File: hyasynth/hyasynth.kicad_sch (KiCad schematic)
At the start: 38 parts, among them J1 Conn_01x04_Male, J2 Conn_01x02_Male, J3 Conn_01x07_Male, J4 Conn_01x02_Male, J5 Conn_01x02_Male, J6 AudioJack3_SwitchTR, SW1 Power Switch, SW10 G# Ab, SW11 A, SW12 A# Bb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

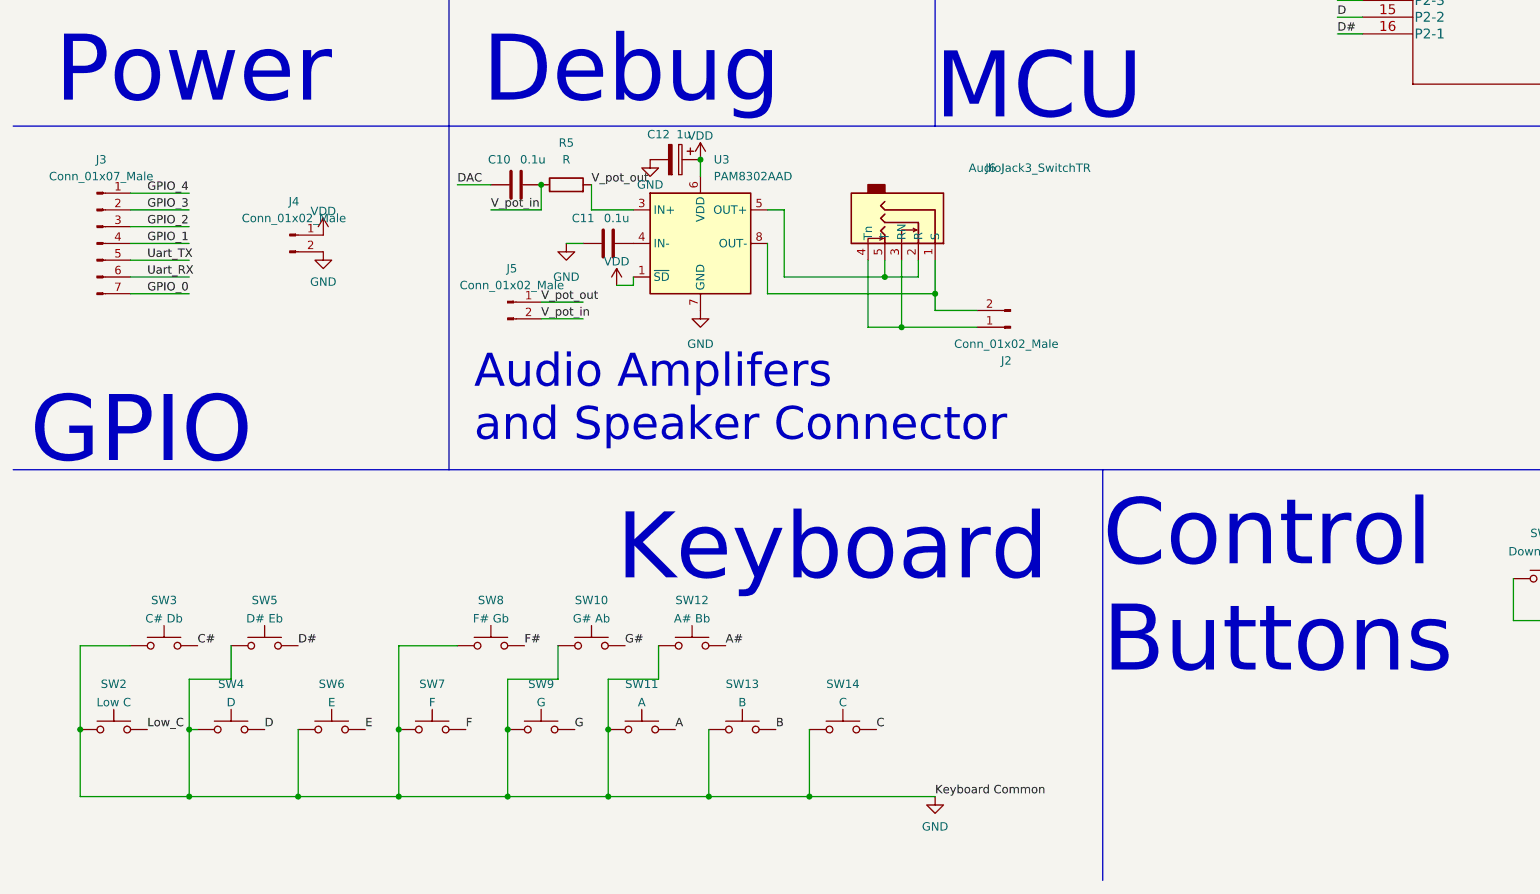
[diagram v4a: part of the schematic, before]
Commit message: Finished Basic Revision of PCB
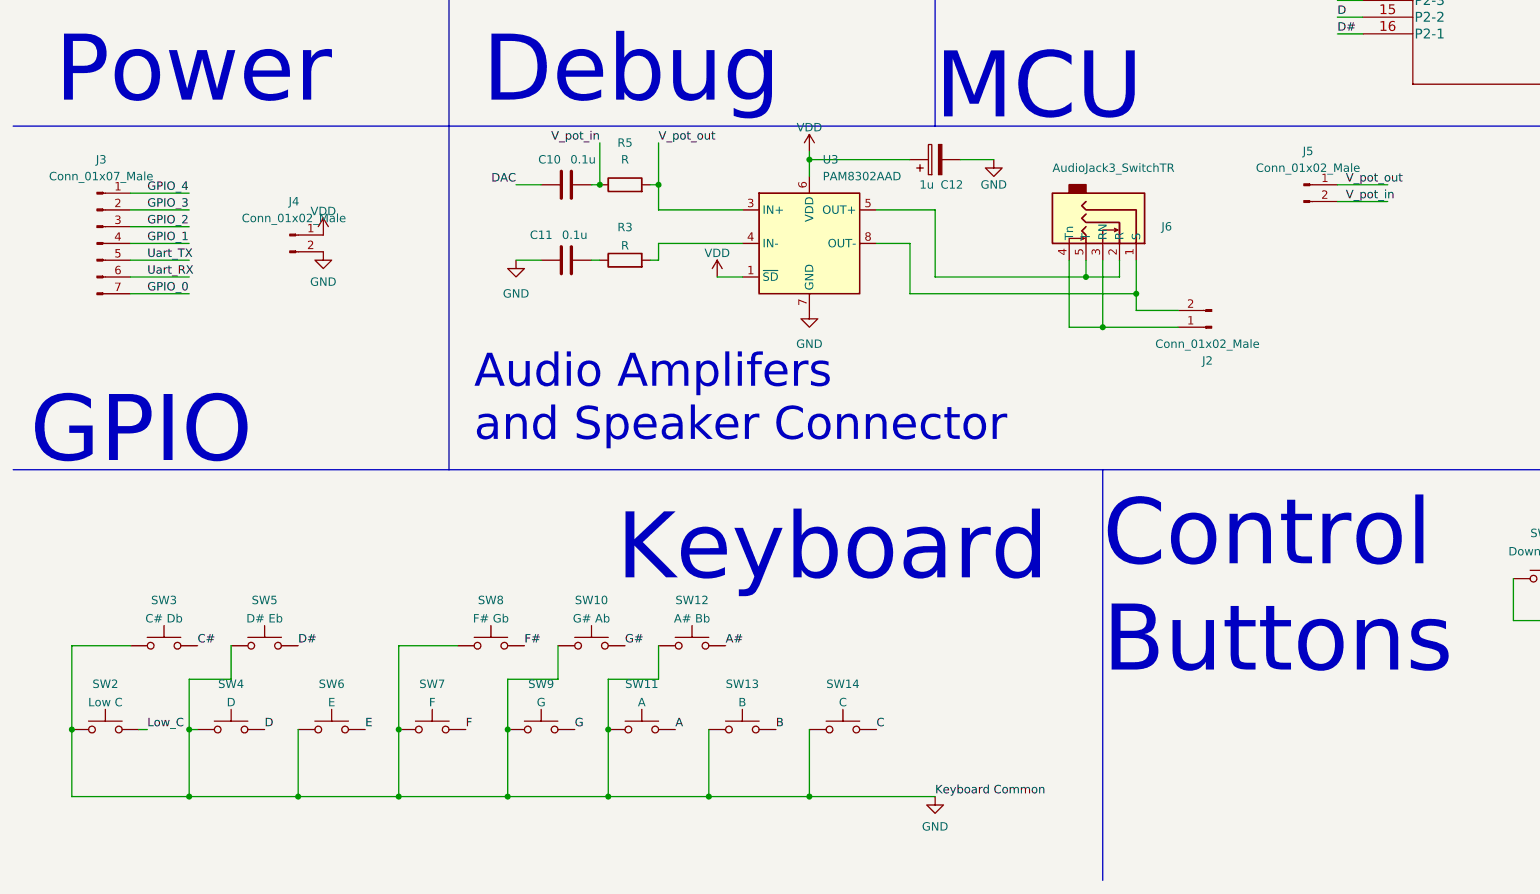
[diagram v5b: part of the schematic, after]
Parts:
- added R3: R, Resistor_SMD:R_0805_2012Metric_Pad1.20x1.40mm_HandSolder, symbol Device:R
- SW10, SW11, SW12, SW13, SW14, SW15, SW16, SW17, SW18, SW2, SW3, SW4, SW5, SW6, SW7, SW8, SW9: footprint Button_Switch_SMD:SW_Push_1P1T_NO_CK_KSC7xxJ -> Button:SW_Push_hand_solder
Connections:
- net at C11.2: now also R3.1; no longer U3.4 (IN-)
- new net: R3.2, U3.4 (IN-)
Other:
- moved on the sheet: C10, C11, C12, J2, J5, J6, R5, SW2, U3

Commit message: Schematic Changes
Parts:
- removed R1: 10K, Resistor_SMD:R_0805_2012Metric_Pad1.20x1.40mm_HandSolder, symbol Device:R
- removed R2: 1K, Resistor_SMD:R_0805_2012Metric_Pad1.20x1.40mm_HandSolder, symbol Device:R
- removed SW18: Reset, Button:SW_Push_hand_solder, symbol Switch:SW_Push
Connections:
- net GND: no longer U1.9 (P3-1)
- net VDD: no longer U3.1 (~{SD})
- net AMP_OUT-: now reaches J2.2 (Pin_2), J6.1 (S), U3.8 (OUT-)
- net AMP_OUT+: now reaches J6.2 (R), J6.5 (T), U3.5 (OUT+)
- net SPK_OUT-: now reaches J2.1 (Pin_1), J6.3 (RN), J6.4 (Tn)
- new net AMP_SD: U1.9 (P3-1), U3.1 (~{SD})

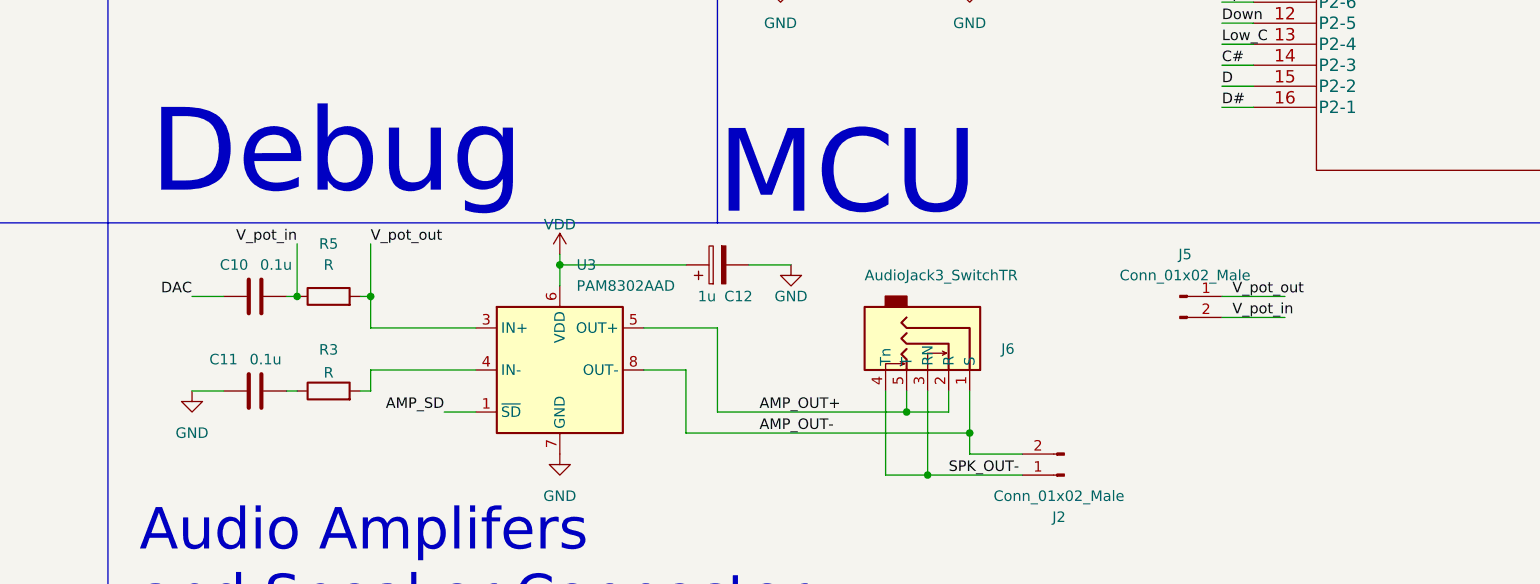
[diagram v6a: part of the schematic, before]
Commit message: tweaks for printing
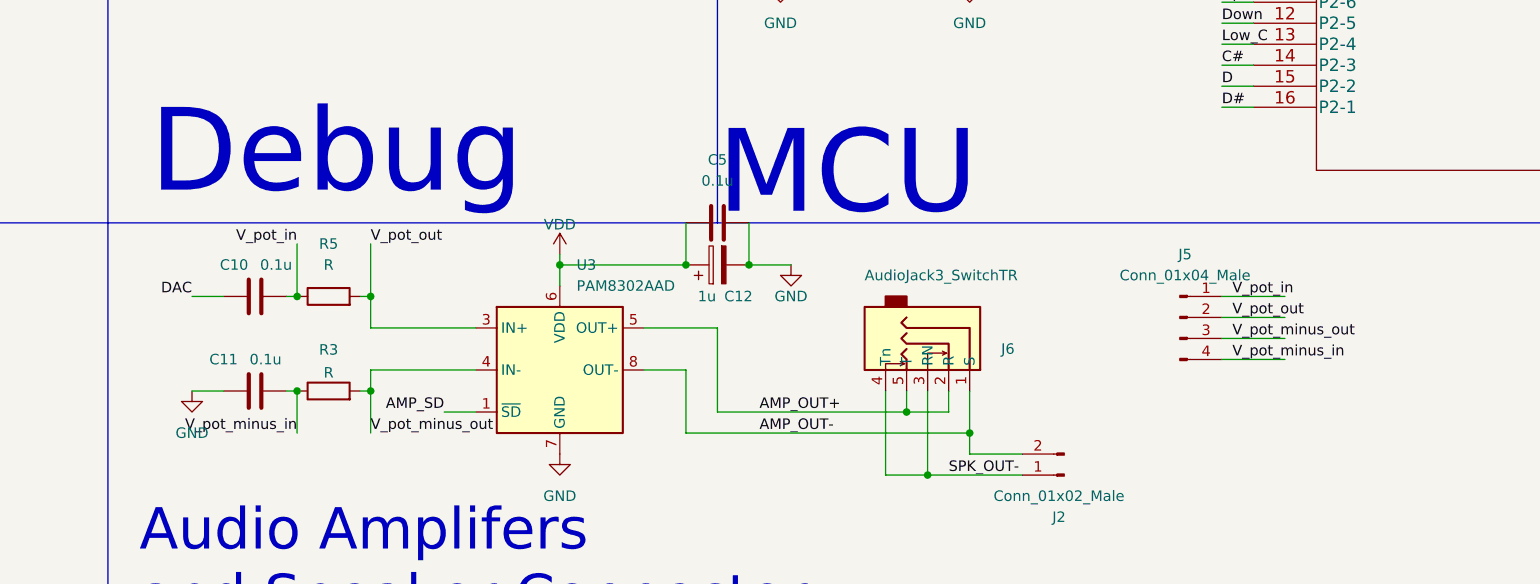
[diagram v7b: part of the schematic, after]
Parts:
- removed J5: Conn_01x02_Male, Connector_PinHeader_2.54mm:PinHeader_1x02_P2.54mm_Vertical, symbol Connector:Conn_01x02_Male
- added C5: 0.1u, Capacitor_SMD:C_0805_2012Metric_Pad1.18x1.45mm_HandSolder, symbol Device:C
- added J5: Conn_01x04_Male, Connector_PinHeader_2.54mm:PinHeader_1x04_P2.54mm_Vertical, symbol Connector:Conn_01x04_Male
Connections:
- net GND: now also C5.2
- net VDD: now also C5.1
- net V_pot_in: now also J5.1 (Pin_1)
- net V_pot_out: now also J5.2 (Pin_2)
- net V_pot_minus_in: now reaches C11.2, R3.1
- net V_pot_minus_in: now also J5.4 (Pin_4)
- net V_pot_minus_out: now reaches R3.2, U3.4 (IN-)
- net V_pot_minus_out: now also J5.3 (Pin_3)
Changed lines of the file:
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@@
   (junction (at 132.08 185.42) (diameter 0) (color 0 0 0 0)
   )
+  (junction (at 154.94 88.9) (diameter 0) (color 0 0 0 0)
+  )
   (junction (at 176.53 114.3) (diameter 0) (color 0 0 0 0)
   )
@@
   (junction (at 20.32 175.26) (diameter 0) (color 0 0 0 0)
   )
+  (junction (at 100.33 104.14) (diameter 0) (color 0 0 0 0)
+  )
   (junction (at 69.85 175.26) (diameter 0) (color 0 0 0 0)
   )
@@
   (junction (at 181.61 48.26) (diameter 0) (color 0 0 0 0)
   )
+  (junction (at 147.32 88.9) (diameter 0) (color 0 0 0 0)
+  )
   (junction (at 101.6 185.42) (diameter 0) (color 0 0 0 0)
   )
@@
   (junction (at 86.36 175.26) (diameter 0) (color 0 0 0 0)
   )
+  (junction (at 109.22 104.14) (diameter 0) (color 0 0 0 0)
+  )
   (junction (at 100.33 92.71) (diameter 0) (color 0 0 0 0)
   )
@@
     (stroke (width 0) (type default) (color 0 0 0 0))
   )
+  (wire (pts (xy 109.22 104.14) (xy 109.22 109.22))
+    (stroke (width 0) (type default) (color 0 0 0 0))
+  )
   (wire (pts (xy 173.99 106.68) (xy 179.07 106.68))
     (stroke (width 0) (type default) (color 0 0 0 0))
@@
     (stroke (width 0) (type default) (color 0 0 0 0))
   )
+  (wire (pts (xy 147.32 83.82) (xy 147.32 88.9))
+    (stroke (width 0) (type default) (color 0 0 0 0))
+  )
   (wire (pts (xy 181.61 40.64) (xy 193.04 40.64))
     (stroke (width 0) (type default) (color 0 0 0 0))
@@
     (stroke (width 0) (type default) (color 0 0 0 0))
   )
+  (wire (pts (xy 100.33 104.14) (xy 100.33 109.22))
+    (stroke (width 0) (type default) (color 0 0 0 0))
+  )
   (wire (pts (xy 158.75 40.64) (xy 170.18 40.64))
     (stroke (width 0) (type default) (color 0 0 0 0))
@@
     (stroke (width 0) (type default) (color 0 0 0 0))
   )
+  (wire (pts (xy 154.94 83.82) (xy 154.94 88.9))
+    (stroke (width 0) (type default) (color 0 0 0 0))
+  )
   (wire (pts (xy 212.09 44.45) (xy 215.9 44.45))
     (stroke (width 0) (type default) (color 0 0 0 0))
@@
     (stroke (width 0) (type default) (color 0 0 0 0))
   )
+  (wire (pts (xy 212.09 97.79) (xy 219.71 97.79))
+    (stroke (width 0) (type default) (color 0 0 0 0))
+  )
   (wire (pts (xy 187.96 111.76) (xy 181.61 111.76))
     (stroke (width 0) (type default) (color 0 0 0 0))
@@
   )
   (wire (pts (xy 99.06 92.71) (xy 100.33 92.71))
+    (stroke (width 0) (type default) (color 0 0 0 0))
+  )
+  (wire (pts (xy 212.09 100.33) (xy 219.71 100.33))
     (stroke (width 0) (type default) (color 0 0 0 0))
   )
@@
     (effects (font (size 1.27 1.27)) (justify right bottom))
   )
+  (label "V_pot_minus_in" (at 100.33 109.22 180)
+    (effects (font (size 1.27 1.27)) (justify right bottom))
+  )
   (label "A#" (at 266.7 57.15 0)
     (effects (font (size 1.27 1.27)) (justify left bottom))
@@
     (effects (font (size 1.27 1.27)) (justify left bottom))
   )
+  (label "V_pot_minus_in" (at 213.36 100.33 0)
+    (effects (font (size 1.27 1.27)) (justify left bottom))
+  )
   (label "AMP_OUT-" (at 156.21 109.22 0)
     (effects (font (size 1.27 1.27)) (justify left bottom))
@@
     (effects (font (size 1.27 1.27)) (justify left bottom))
   )
+  (label "V_pot_minus_out" (at 109.22 109.22 0)
+    (effects (font (size 1.27 1.27)) (justify left bottom))
+  )
   (label "D#" (at 212.09 69.85 0)
     (effects (font (size 1.27 1.27)) (justify left bottom))
@@
   )
   (label "A" (at 111.76 175.26 0)
+    (effects (font (size 1.27 1.27)) (justify left bottom))
+  )
+  (label "V_pot_minus_out" (at 213.36 97.79 0)
     (effects (font (size 1.27 1.27)) (justify left bottom))
   )
@@
     (effects (font (size 1.27 1.27)) (justify right bottom))
   )
-  (label "V_pot_out" (at 213.36 92.71 0)
+  (label "V_pot_out" (at 213.36 95.25 0)
     (effects (font (size 1.27 1.27)) (justify left bottom))
   )
@@
     (effects (font (size 1.27 1.27)) (justify left bottom))
   )
-  (label "V_pot_in" (at 213.36 95.25 0)
+  (label "V_pot_in" (at 213.36 92.71 0)
     (effects (font (size 1.27 1.27)) (justify left bottom))
   )
@@
     (pin "1")
   )
+  (symbol (lib_id "Device:C") (at 151.13 83.82 90) (unit 1)
+    (in_bom yes) (on_board yes) (fields_autoplaced)
+    (property "Reference" "C5" (id 0) (at 151.13 76.2 90))
+    (property "Value" "0.1u" (id 1) (at 151.13 78.74 90))
+    (property "Footprint" "Capacitor_SMD:C_0805_2012Metric_Pad1.18x1.45mm_HandSolder" (id 2) (at 154.94 82.8548 0)
+      (effects (font (size 1.27 1.27)) hide)
+    )
+    (property "Datasheet" "~" (id 3) (at 151.13 83.82 0)
+      (effects (font (size 1.27 1.27)) hide)
+    )
+    (pin "1")
+    (pin "2")
+  )
   (symbol (lib_id "Device:R") (at 104.14 104.14 90) (unit 1)
     (in_bom yes) (on_board yes) (fields_autoplaced)
@@
     )
     (pin "1")
-  )
-  (symbol (lib_id "Connector:Conn_01x02_Male") (at 207.01 92.71 0) (unit 1)
-    (in_bom yes) (on_board yes) (fields_autoplaced)
-    (property "Reference" "J5" (id 0) (at 207.645 87.63 0))
-    (property "Value" "Conn_01x02_Male" (id 1) (at 207.645 90.17 0))
-    (property "Footprint" "Connector_PinHeader_2.54mm:PinHeader_1x02_P2.54mm_Vertical" (id 2) (at 207.01 92.71 0)
-      (effects (font (size 1.27 1.27)) hide)
-    )
-    (property "Datasheet" "~" (id 3) (at 207.01 92.71 0)
-      (effects (font (size 1.27 1.27)) hide)
-    )
-    (pin "1")
-    (pin "2")
   )
   (symbol (lib_id "Switch:SW_Push") (at 121.92 175.26 0) (unit 1)
@@
     (pin "1")
   )
+  (symbol (lib_id "Connector:Conn_01x04_Male") (at 207.01 95.25 0) (unit 1)
+    (in_bom yes) (on_board yes) (fields_autoplaced)
+    (property "Reference" "J5" (id 0) (at 207.645 87.63 0))
+    (property "Value" "Conn_01x04_Male" (id 1) (at 207.645 90.17 0))
+    (property "Footprint" "Connector_PinHeader_2.54mm:PinHeader_1x04_P2.54mm_Vertical" (id 2) (at 207.01 95.25 0)
+      (effects (font (size 1.27 1.27)) hide)
+    )
+    (property "Datasheet" "~" (id 3) (at 207.01 95.25 0)
+      (effects (font (size 1.27 1.27)) hide)
+    )
+    (pin "1")
+    (pin "2")
+    (pin "3")
+    (pin "4")
+  )
   (symbol (lib_id "Device:C") (at 170.18 44.45 0) (unit 1)
     (in_bom yes) (on_board yes) (fields_autoplaced)
@@
       (reference "C4") (unit 1) (value "0.1u") (footprint "Capacitor_SMD:C_0805_2012Metric_Pad1.18x1.45mm_HandSolder")
     )
+    (path "/518a24d0-27c5-426e-940c-a357429cad49"
+      (reference "C5") (unit 1) (value "0.1u") (footprint "Capacitor_SMD:C_0805_2012Metric_Pad1.18x1.45mm_HandSolder")
+    )
     (path "/b7a6bb1f-8fe6-40d7-91b8-592d0ab889d4"
       (reference "C10") (unit 1) (value "0.1u") (footprint "Capacitor_SMD:C_0805_2012Metric_Pad1.18x1.45mm_HandSolder")
@@
       (reference "J4") (unit 1) (value "Conn_01x02_Male") (footprint "Connector_PinHeader_2.54mm:PinHeader_1x02_P2.54mm_Vertical")
     )
-    (path "/6bd9e2e6-f880-4b95-abeb-a7779526b27c"
-      (reference "J5") (unit 1) (value "Conn_01x02_Male") (footprint "Connector_PinHeader_2.54mm:PinHeader_1x02_P2.54mm_Vertical")
+    (path "/f96df586-90b1-4dc4-869b-df72f115a13d"
+      (reference "J5") (unit 1) (value "Conn_01x04_Male") (footprint "Connector_PinHeader_2.54mm:PinHeader_1x04_P2.54mm_Vertical")
     )
     (path "/302f71e7-221e-4108-92c1-cb6009e0ebe5"

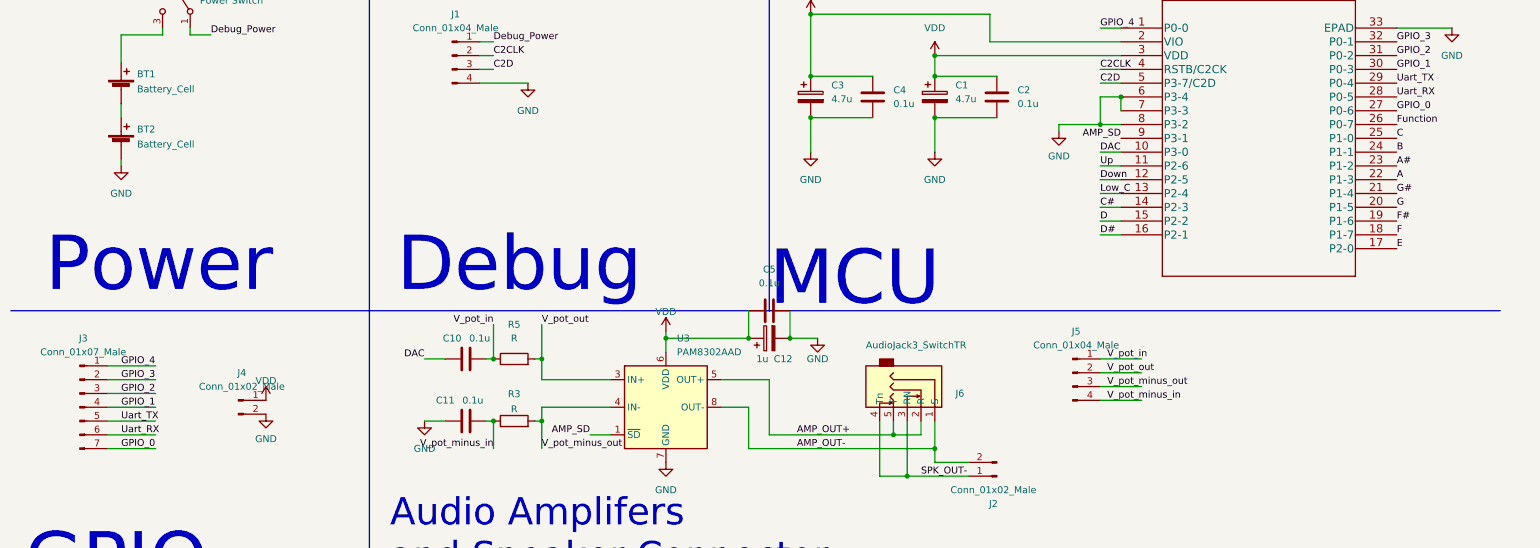
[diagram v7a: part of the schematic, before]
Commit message: added headphone resistor, moved amp SD pin, tweak hole size
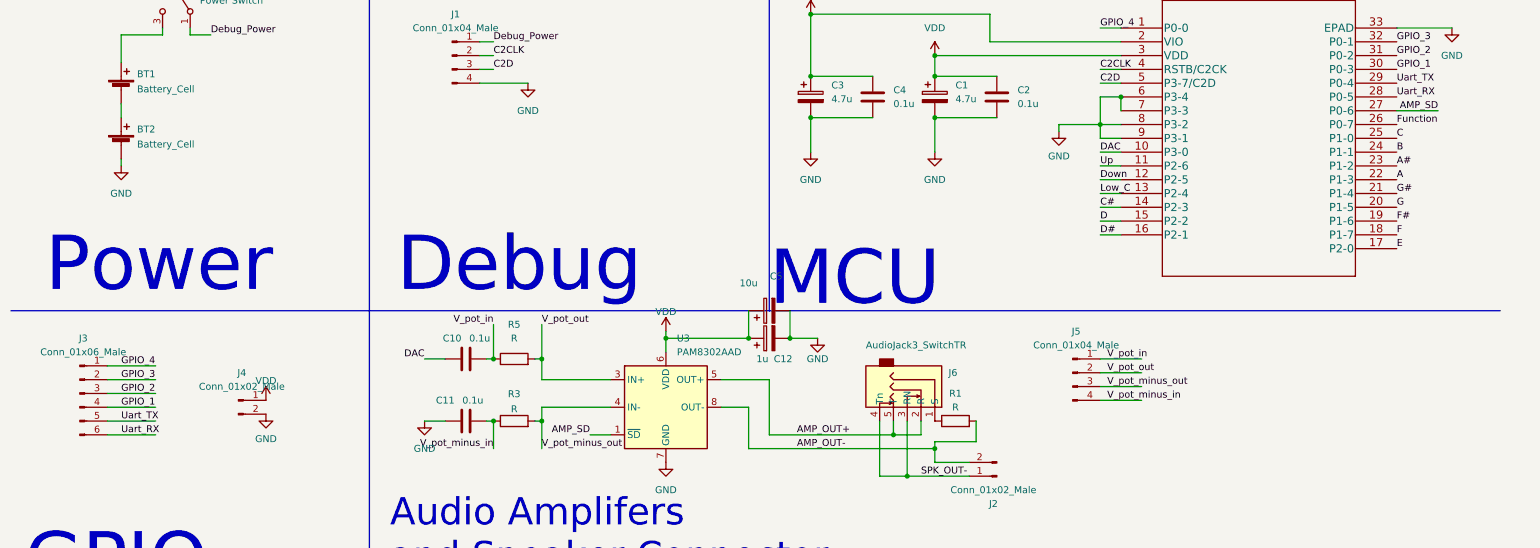
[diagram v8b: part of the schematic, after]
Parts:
- removed C5: 0.1u, Capacitor_SMD:C_0805_2012Metric_Pad1.18x1.45mm_HandSolder, symbol Device:C
- removed J3: Conn_01x07_Male, Connector_PinHeader_2.54mm:PinHeader_1x07_P2.54mm_Vertical, symbol Connector:Conn_01x07_Male
- added C5: 10u, Capacitor_Tantalum_SMD:CP_EIA-7343-31_Kemet-D_Pad2.25x2.55mm_HandSolder, symbol Device:C_Polarized
- added J3: Conn_01x06_Male, Connector_PinHeader_2.54mm:PinHeader_1x06_P2.54mm_Vertical, symbol Connector:Conn_01x06_Male
- added R1: R, Resistor_SMD:R_0805_2012Metric_Pad1.20x1.40mm_HandSolder, symbol Device:R
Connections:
- net GPIO_0 is gone; now on net AMP_SD: U1.27 (P0-6)
- net AMP_OUT-: now also R1.2; no longer J6.1 (S)
- net AMP_SD: no longer U1.9 (P3-1)
- net GND: now also U1.9 (P3-1), C5.2
- net GPIO_1: now also J3.4 (Pin_4)
- net GPIO_2: now also J3.3 (Pin_3)
- net GPIO_3: now also J3.2 (Pin_2)
- net GPIO_4: now also J3.1 (Pin_1)
- net Uart_RX: now also J3.6 (Pin_6)
- net Uart_TX: now also J3.5 (Pin_5)
- net VDD: now also C5.1
- new net: J6.1 (S), R1.1
